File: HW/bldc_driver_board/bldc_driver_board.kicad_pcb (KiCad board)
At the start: 2 copper layers, 80 x 119.4 mm, 53 parts, among them IC1 DRV8305NPHPR, J1 PWR, J2 N_CN7, J3 N_CN10, J4 HALL, J5 Motor, J6 RJ45, J7 RJ45, Q1 STD140N6F7, Q2 STD140N6F7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

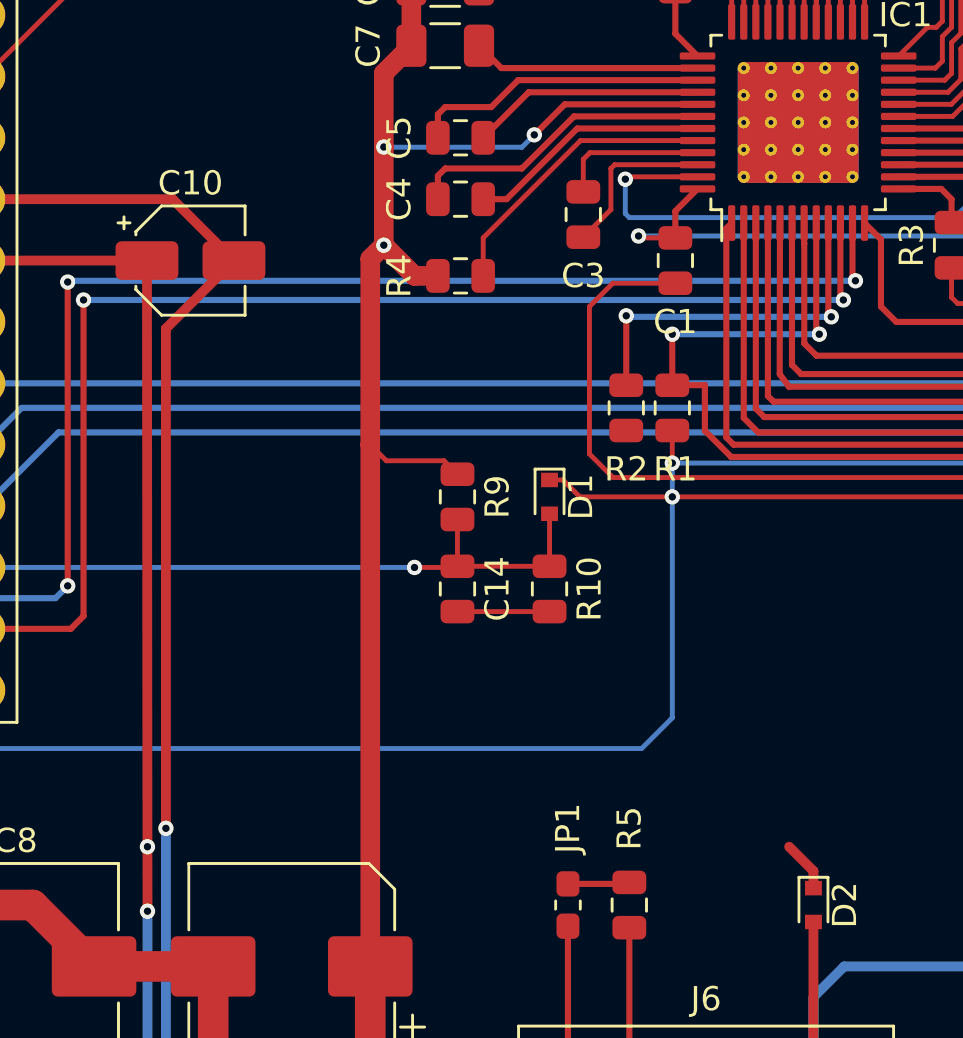
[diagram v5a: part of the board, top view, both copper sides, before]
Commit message: -- Fixed loose wire
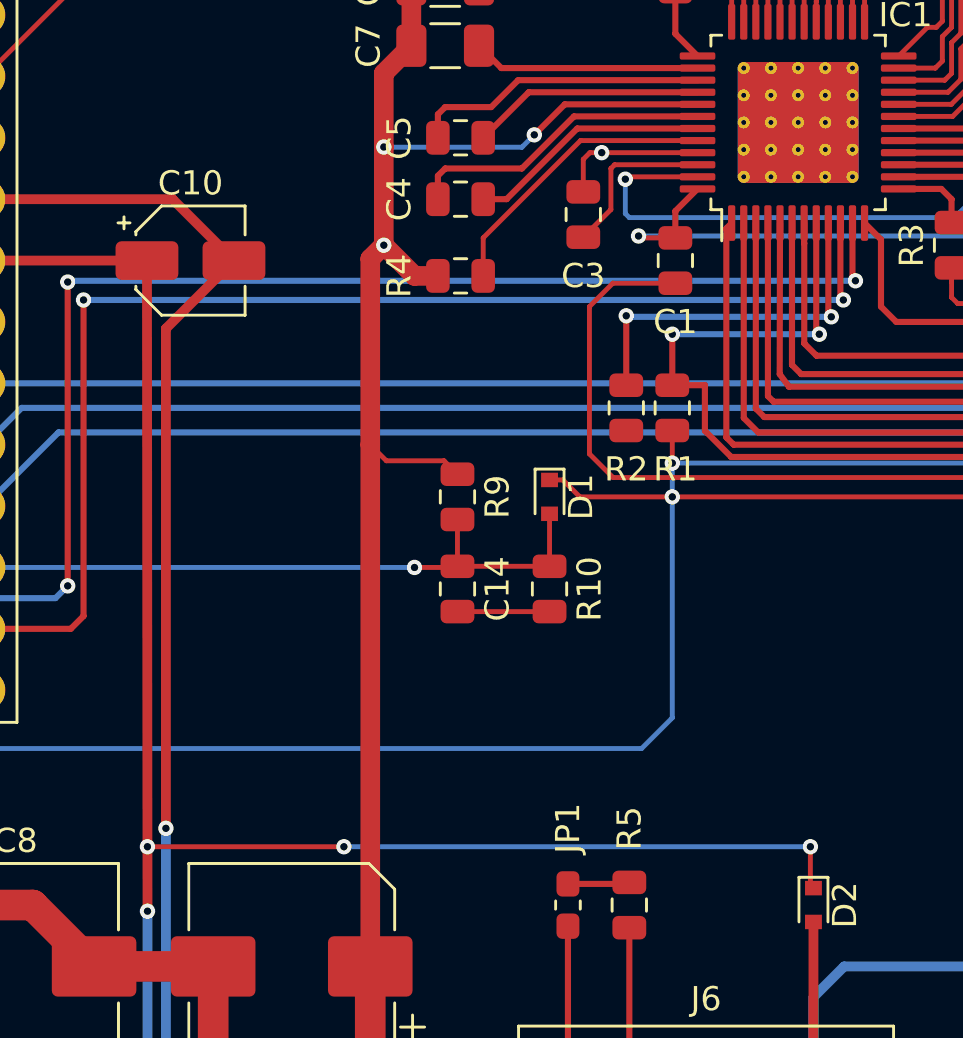
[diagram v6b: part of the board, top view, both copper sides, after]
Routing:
- net +12V: track 50.5 -> 77.6 mm, vias 2 -> 4
- net GND: vias 3 -> 4
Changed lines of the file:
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@@
     (thickness 1.6)
     (drawings 4)
-    (tracks 696)
+    (tracks 702)
     (zones 0)
     (modules 53)
@@
   )
   (setup
-    (last_trace_width 1.27)
+    (last_trace_width 0.2032)
     (user_trace_width 0.2032)
     (user_trace_width 0.254)
@@
   (segment (start 53.213 119.656) (end 56.029 116.84) (width 0.4064) (layer F.Cu) (net 4))
   (segment (start 53.213 140.335) (end 53.213 119.656) (width 0.4064) (layer F.Cu) (net 4))
-  (segment (start 75.2125 112.375) (end 70.759 112.375) (width 0.2032) (layer F.Cu) (net 4))
+  (segment (start 75.2125 112.375) (end 71.247 112.375) (width 0.2032) (layer F.Cu) (net 4))
   (segment (start 70.485 112.649) (end 70.485 113.9975) (width 0.2032) (layer F.Cu) (net 4))
   (segment (start 70.759 112.375) (end 70.485 112.649) (width 0.2032) (layer F.Cu) (net 4))
@@
   (segment (start 60.706 86.36) (end 38.481 86.36) (width 1.27) (layer F.Cu) (net 4))
   (segment (start 38.481 86.36) (end 36.83 88.011) (width 1.27) (layer F.Cu) (net 4))
+  (segment (start 71.247 112.375) (end 70.759 112.375) (width 0.2032) (layer F.Cu) (net 4))
+  (via (at 71.247 112.375) (size 0.635) (drill 0.3048) (layers F.Cu B.Cu) (net 4))
   (segment (start 75.2125 112.875) (end 71.783 112.875) (width 0.2032) (layer F.Cu) (net 5))
   (segment (start 71.783 112.875) (end 71.628 113.03) (width 0.2032) (layer F.Cu) (net 5))
@@
   (segment (start 52.448821 141.097) (end 52.448821 141.097) (width 0.4064) (layer F.Cu) (net 12))
   (via (at 52.448821 141.097) (size 0.635) (drill 0.3048) (layers F.Cu B.Cu) (net 12))
-  (segment (start 80.01 142.81) (end 80.01 142.1036) (width 0.4064) (layer F.Cu) (net 12))
-  (segment (start 80.01 142.1036) (end 79.0034 141.097) (width 0.4064) (layer F.Cu) (net 12))
+  (via (at 60.579 141.097) (size 0.635) (drill 0.3048) (layers F.Cu B.Cu) (net 12))
+  (segment (start 52.448821 141.097) (end 60.579 141.097) (width 0.2032) (layer F.Cu) (net 12))
+  (via (at 79.883 141.097) (size 0.635) (drill 0.3048) (layers F.Cu B.Cu) (net 12))
+  (segment (start 60.579 141.097) (end 79.883 141.097) (width 0.2032) (layer B.Cu) (net 12))
+  (segment (start 79.883 142.683) (end 80.01 142.81) (width 0.2032) (layer F.Cu) (net 12))
+  (segment (start 79.883 141.097) (end 79.883 142.683) (width 0.2032) (layer F.Cu) (net 12))
   (segment (start 74.295 107.4575) (end 74.295 105.7125) (width 0.254) (layer F.Cu) (net 13))
   (segment (start 75.2125 108.375) (end 74.295 107.4575) (width 0.254) (layer F.Cu) (net 13))

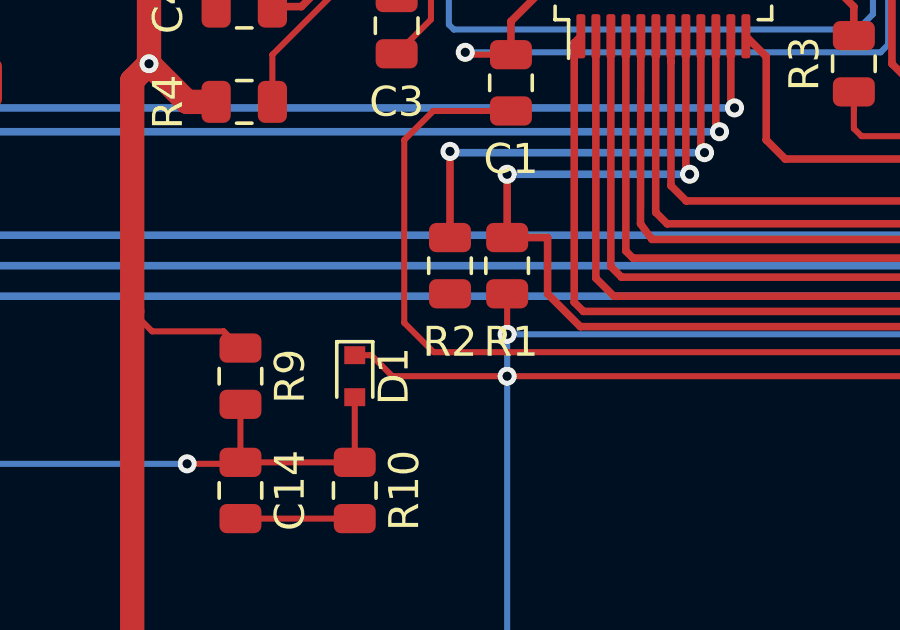
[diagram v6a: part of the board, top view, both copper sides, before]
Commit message: -- Fixed ground connection
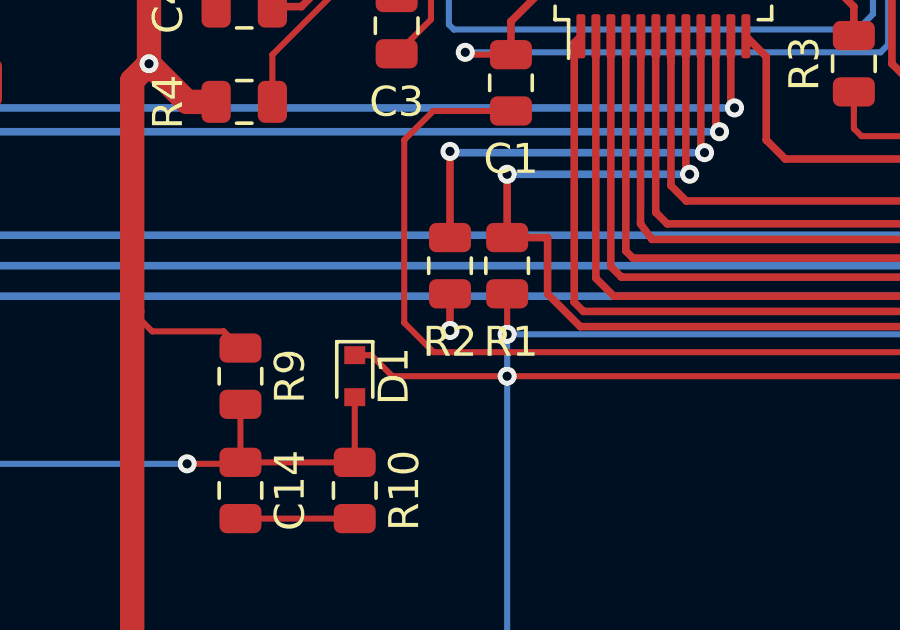
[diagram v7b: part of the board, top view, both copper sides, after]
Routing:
- net GND: track 342.3 -> 343.5 mm, vias 4 -> 5
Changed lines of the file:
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@@
     (thickness 1.6)
     (drawings 4)
-    (tracks 702)
+    (tracks 704)
     (zones 0)
     (modules 53)
@@
   )
   (setup
-    (last_trace_width 0.2032)
+    (last_trace_width 0.254)
     (user_trace_width 0.2032)
     (user_trace_width 0.254)
@@
   (segment (start 71.247 112.375) (end 70.759 112.375) (width 0.2032) (layer F.Cu) (net 4))
   (via (at 71.247 112.375) (size 0.635) (drill 0.3048) (layers F.Cu B.Cu) (net 4))
+  (via (at 72.263 125.095) (size 0.635) (drill 0.3048) (layers F.Cu B.Cu) (net 4))
+  (segment (start 72.263 123.8735) (end 72.263 125.095) (width 0.254) (layer F.Cu) (net 4))
   (segment (start 75.2125 112.875) (end 71.783 112.875) (width 0.2032) (layer F.Cu) (net 5))
   (segment (start 71.783 112.875) (end 71.628 113.03) (width 0.2032) (layer F.Cu) (net 5))
@@
   (segment (start 46.615 60.7) (end 46.615 66.92) (width 1.27) (layer F.Cu) (net 46))
   (segment (start 50.165 57.15) (end 46.615 60.7) (width 1.27) (layer F.Cu) (net 46))
-  (segment (start 58.42 64.55) (end 58.42 69.02) (width 1.27) (layer F.Cu) (net 46))
-  (segment (start 57.624 63.754) (end 58.42 64.55) (width 1.27) (layer F.Cu) (net 46))
-  (segment (start 53.213 63.754) (end 57.624 63.754) (width 1.27) (layer F.Cu) (net 46))
-  (segment (start 50.165 60.706) (end 53.213 63.754) (width 1.27) (layer F.Cu) (net 46))
   (segment (start 50.165 57.15) (end 50.165 60.706) (width 1.27) (layer F.Cu) (net 46))
   (segment (start 77.125 100.589171) (end 76.611829 100.076) (width 0.2032) (layer F.Cu) (net 46))
@@
   (segment (start 58.293 84.709) (end 58.293 75.447) (width 0.2032) (layer F.Cu) (net 46))
   (segment (start 58.42 69.02) (end 58.42 75.32) (width 1.27) (layer F.Cu) (net 46))
+  (segment (start 50.165 60.706) (end 53.213 63.754) (width 1.27) (layer F.Cu) (net 46))
+  (segment (start 53.213 63.754) (end 57.624 63.754) (width 1.27) (layer F.Cu) (net 46))
+  (segment (start 58.42 64.55) (end 58.42 69.02) (width 1.27) (layer F.Cu) (net 46))
+  (segment (start 57.624 63.754) (end 58.42 64.55) (width 1.27) (layer F.Cu) (net 46))
   (segment (start 51.9782 66.92) (end 52.705 67.6468) (width 0.2032) (layer F.Cu) (net 47))
   (segment (start 51.175 66.92) (end 51.9782 66.92) (width 0.2032) (layer F.Cu) (net 47))

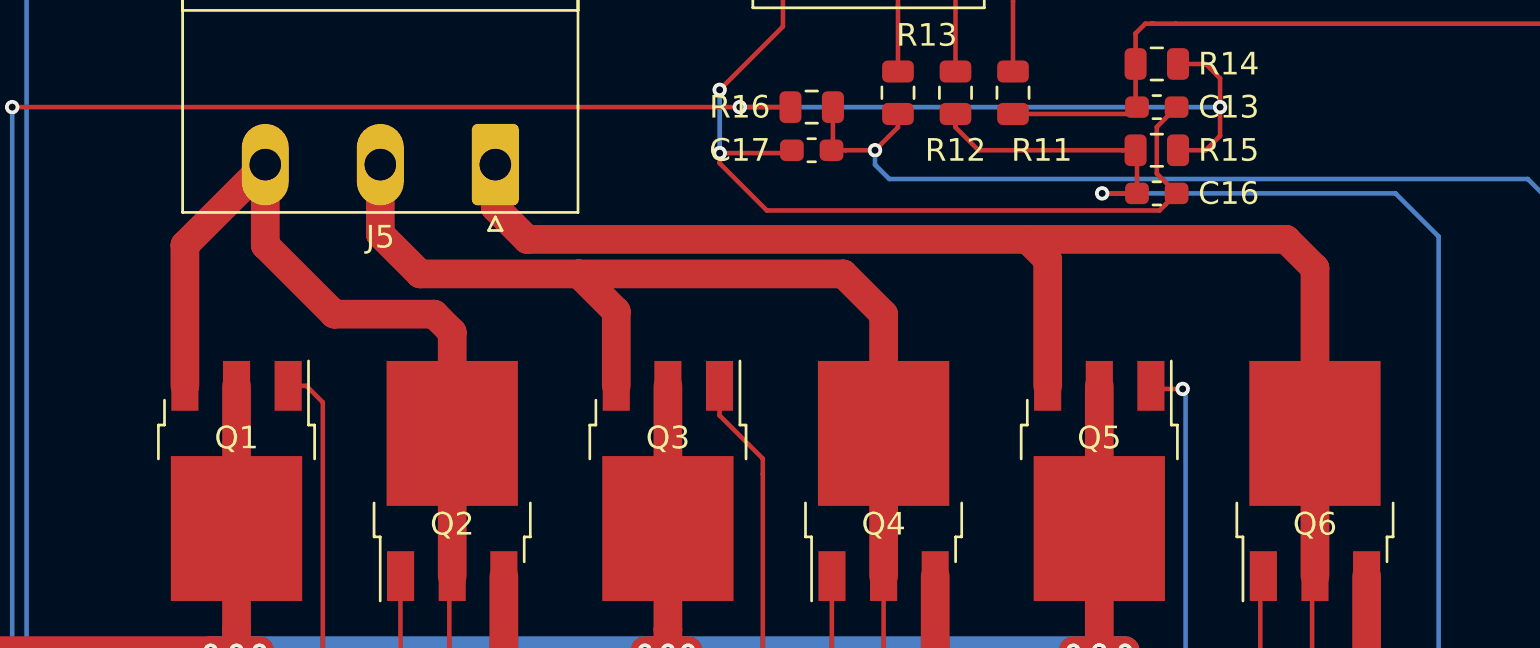
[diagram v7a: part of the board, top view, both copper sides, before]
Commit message: -- Added fields for BLDC output
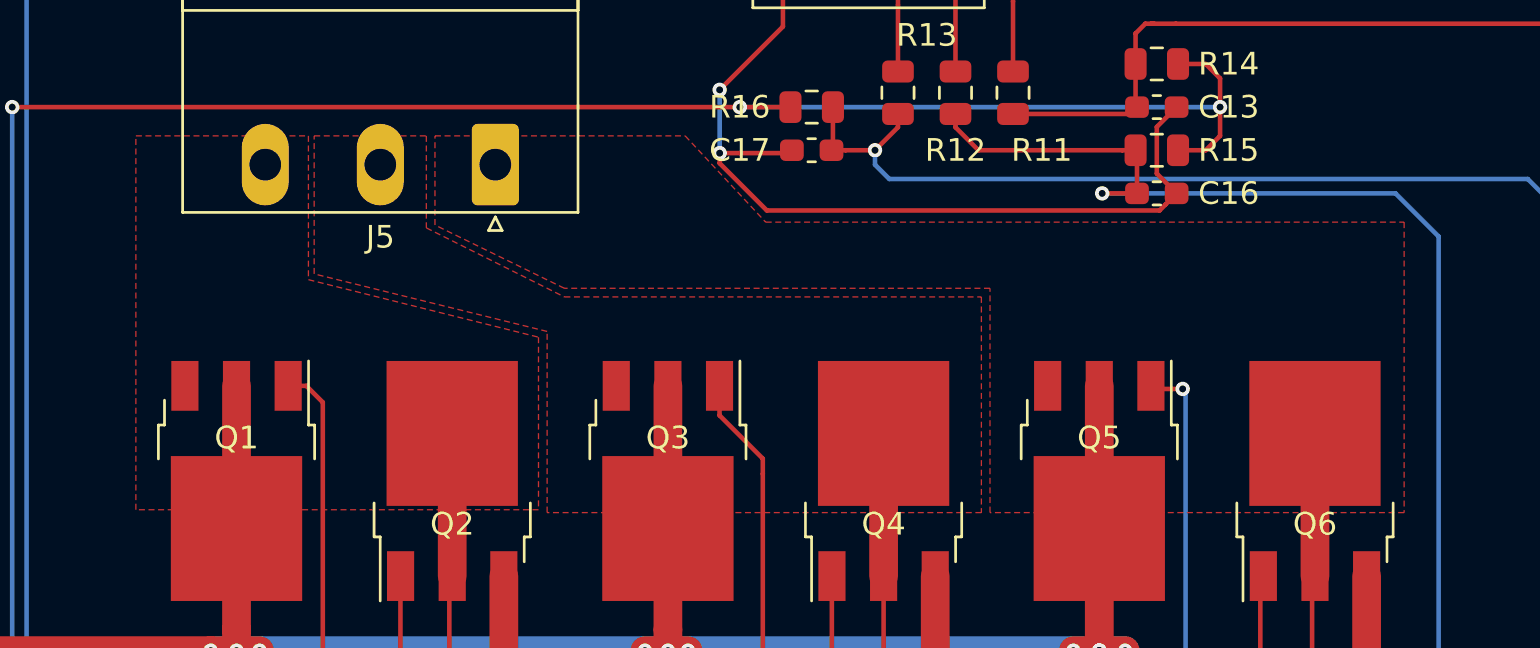
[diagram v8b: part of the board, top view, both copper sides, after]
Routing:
- net /SHC: track 105.2 -> 51.9 mm
- net /SHB: track 77.9 -> 40.3 mm
- net /SHA: track 85.3 -> 56.2 mm
- added copper zone on F.Cu, net /SHA
- added copper zone on F.Cu, net /SHB
- added copper zone on F.Cu, net /SHC
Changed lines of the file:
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@@
     (thickness 1.6)
     (drawings 4)
-    (tracks 704)
+    (tracks 681)
     (zones 0)
     (modules 53)
@@
   (segment (start 94.107 75.453) (end 94.24 75.32) (width 0.2032) (layer F.Cu) (net 39))
   (segment (start 94.107 84.836) (end 94.107 75.453) (width 0.2032) (layer F.Cu) (net 39))
-  (segment (start 84.715 61.347) (end 84.715 66.92) (width 1.27) (layer F.Cu) (net 40))
-  (segment (start 83.82 60.452) (end 84.715 61.347) (width 1.27) (layer F.Cu) (net 40))
-  (segment (start 61.727 60.452) (end 83.82 60.452) (width 1.27) (layer F.Cu) (net 40))
-  (segment (start 60.325 57.15) (end 60.325 59.05) (width 1.27) (layer F.Cu) (net 40))
-  (segment (start 60.325 59.05) (end 61.727 60.452) (width 1.27) (layer F.Cu) (net 40))
-  (segment (start 96.52 61.722) (end 96.52 69.02) (width 1.27) (layer F.Cu) (net 40))
-  (segment (start 83.82 60.452) (end 95.25 60.452) (width 1.27) (layer F.Cu) (net 40))
-  (segment (start 95.25 60.452) (end 96.52 61.722) (width 1.27) (layer F.Cu) (net 40))
   (segment (start 81.125 106.9625) (end 81.125 90.833) (width 0.2032) (layer F.Cu) (net 40))
   (via (at 96.393 88.519) (size 0.635) (drill 0.3048) (layers F.Cu B.Cu) (net 40))
@@
   (segment (start 72.136 89.281) (end 72.771 89.916) (width 0.2032) (layer B.Cu) (net 42))
   (segment (start 55.245 57.15) (end 55.245 57.91) (width 1.27) (layer F.Cu) (net 43))
-  (segment (start 55.245 60.22) (end 57.001 61.976) (width 1.27) (layer F.Cu) (net 43))
-  (segment (start 55.245 57.15) (end 55.245 60.22) (width 1.27) (layer F.Cu) (net 43))
-  (segment (start 57.001 61.976) (end 64.008 61.976) (width 1.27) (layer F.Cu) (net 43))
-  (segment (start 65.665 63.633) (end 65.665 66.92) (width 1.27) (layer F.Cu) (net 43))
-  (segment (start 64.008 61.976) (end 65.665 63.633) (width 1.27) (layer F.Cu) (net 43))
-  (segment (start 77.47 63.754) (end 77.47 69.02) (width 1.27) (layer F.Cu) (net 43))
-  (segment (start 64.008 61.976) (end 75.692 61.976) (width 1.27) (layer F.Cu) (net 43))
-  (segment (start 75.692 61.976) (end 77.47 63.754) (width 1.27) (layer F.Cu) (net 43))
   (via (at 77.47 87.63) (size 0.635) (drill 0.3048) (layers F.Cu B.Cu) (net 43))
   (segment (start 78.607414 87.63) (end 77.47 87.63) (width 0.2032) (layer F.Cu) (net 43))
@@
   (segment (start 56.134 75.326) (end 56.14 75.32) (width 0.2032) (layer F.Cu) (net 45))
   (segment (start 56.134 81.153) (end 56.134 75.326) (width 0.2032) (layer F.Cu) (net 45))
-  (segment (start 46.615 60.7) (end 46.615 66.92) (width 1.27) (layer F.Cu) (net 46))
-  (segment (start 50.165 57.15) (end 46.615 60.7) (width 1.27) (layer F.Cu) (net 46))
-  (segment (start 50.165 57.15) (end 50.165 60.706) (width 1.27) (layer F.Cu) (net 46))
   (segment (start 77.125 100.589171) (end 76.611829 100.076) (width 0.2032) (layer F.Cu) (net 46))
   (segment (start 77.125 106.9625) (end 77.125 100.589171) (width 0.2032) (layer F.Cu) (net 46))
@@
   (segment (start 58.293 84.709) (end 58.293 75.447) (width 0.2032) (layer F.Cu) (net 46))
   (segment (start 58.42 69.02) (end 58.42 75.32) (width 1.27) (layer F.Cu) (net 46))
-  (segment (start 50.165 60.706) (end 53.213 63.754) (width 1.27) (layer F.Cu) (net 46))
-  (segment (start 53.213 63.754) (end 57.624 63.754) (width 1.27) (layer F.Cu) (net 46))
-  (segment (start 58.42 64.55) (end 58.42 69.02) (width 1.27) (layer F.Cu) (net 46))
-  (segment (start 57.624 63.754) (end 58.42 64.55) (width 1.27) (layer F.Cu) (net 46))
   (segment (start 51.9782 66.92) (end 52.705 67.6468) (width 0.2032) (layer F.Cu) (net 47))
   (segment (start 51.175 66.92) (end 51.9782 66.92) (width 0.2032) (layer F.Cu) (net 47))
@@
   (segment (start 72.3275 142.635) (end 72.39 142.5725) (width 0.254) (layer F.Cu) (net 111))
   (segment (start 69.85 142.635) (end 72.3275 142.635) (width 0.254) (layer F.Cu) (net 111))
+  (zone (net 46) (net_name /SHA) (layer F.Cu) (hatch edge 0.508)
+    (connect_pads (clearance 0.508))
+    (min_thickness 0.254)
+    (fill yes (arc_segments 16) (thermal_gap 0.508) (thermal_bridge_width 0.508))
+    (polygon
+      (pts
+        (xy 44.45 55.88) (xy 52.07 55.88) (xy 52.07 62.23) (xy 62.23 64.77) (xy 62.23 72.39)
+        (xy 44.45 72.39)
+      )
+    )
+  )
+  (zone (net 43) (net_name /SHB) (layer F.Cu) (hatch edge 0.508)
+    (connect_pads (clearance 0.508))
+    (min_thickness 0.254)
+    (fill yes (arc_segments 16) (thermal_gap 0.508) (thermal_bridge_width 0.508))
+    (polygon
+      (pts
+        (xy 52.324 55.88) (xy 57.277 55.88) (xy 57.277 59.944) (xy 63.373 62.992) (xy 81.788 62.992)
+        (xy 81.788 72.517) (xy 62.611 72.517) (xy 62.611 64.516) (xy 52.324 61.976)
+      )
+    )
+  )
+  (zone (net 40) (net_name /SHC) (layer F.Cu) (hatch edge 0.508)
+    (connect_pads (clearance 0.508))
+    (min_thickness 0.254)
+    (fill yes (arc_segments 16) (thermal_gap 0.508) (thermal_bridge_width 0.508))
+    (polygon
+      (pts
+        (xy 57.658 55.88) (xy 68.707 55.88) (xy 72.263 59.69) (xy 100.457 59.69) (xy 100.457 72.517)
+        (xy 82.169 72.517) (xy 82.169 62.611) (xy 63.373 62.611) (xy 57.658 59.817)
+      )
+    )
+  )
 )
